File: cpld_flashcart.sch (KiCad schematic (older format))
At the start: 12 parts, among them J1 Micro_SD_Card, J2 GG_FrontPins, J3 GG_BackPins, J4 Conn_01x10_Female, U1 TXB0104PW, U2 AP2112K-3.3, U3 ATmega4809-A, U4 SST39SF040, U5 ATF1502AS-xAx44

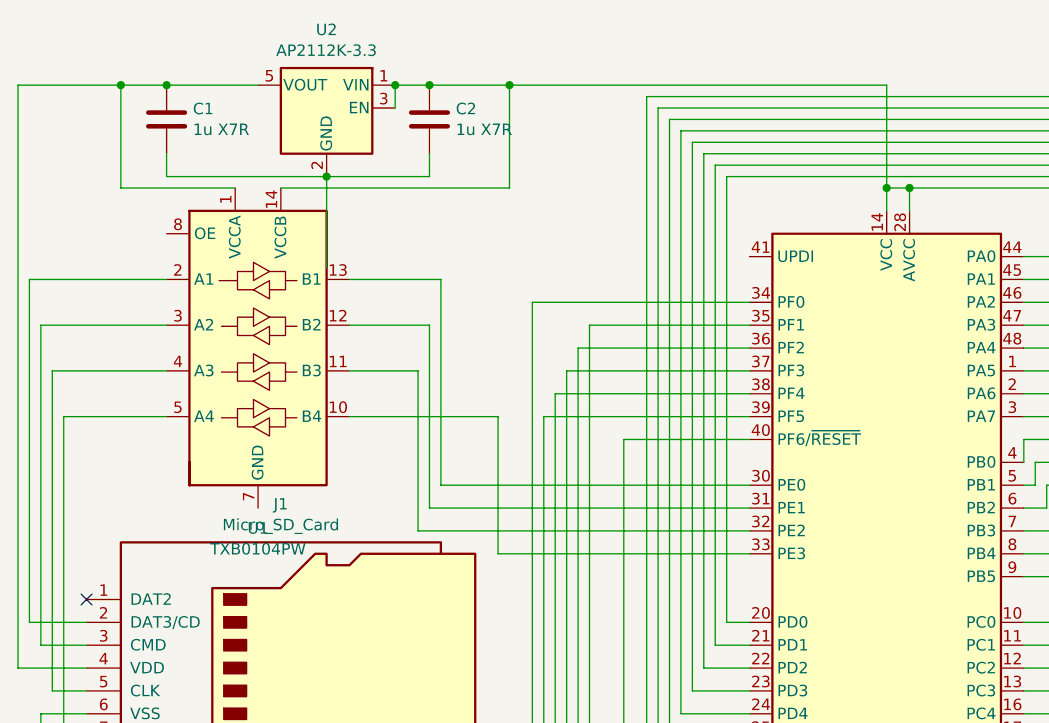
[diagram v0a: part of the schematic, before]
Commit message: Added CUPL code for mapper, and some changes to the schematic (which is definitely still incomplete).
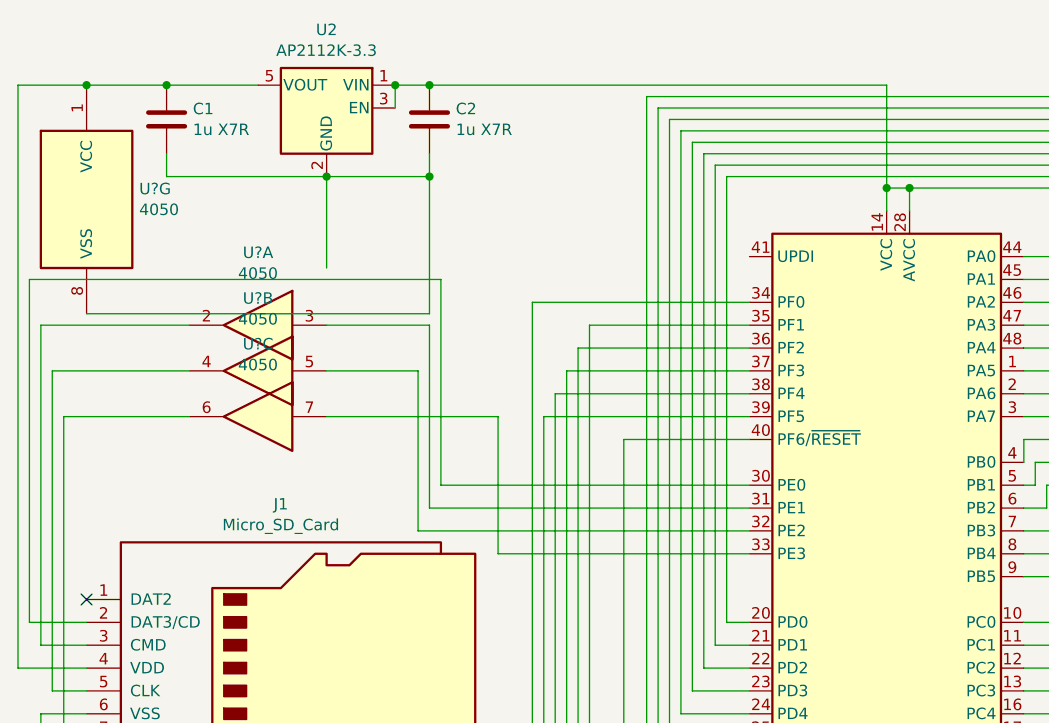
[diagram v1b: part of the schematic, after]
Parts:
- removed U1: TXB0104PW, Package_SO:TSSOP-14_4.4x5mm_P0.65mm, symbol Logic_LevelTranslator:TXB0104PW
- added U? (x4): 4050, symbol 4xxx:4050
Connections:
- net at U3.30 (PE0): now also J1.2 (DAT3/CD)
- net at U3.31 (PE1): now also U?.3
- net at U3.32 (PE2): now also U?.5
- net at U3.33 (PE3): now also U?.7
- net at C1.1, J1.4 (VDD), U2.5 (VOUT): now also U?.1 (VCC)
- net at J1.3 (CMD): now also U?.2
- net at J1.5 (CLK): now also U?.4
- net at J1.7 (DAT0): now also U?.6
- net at C1.2, C2.2, U2.2 (GND): now also U?.8 (VSS)
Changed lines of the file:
@@
 Connection ~ 1150 900
-Wire Wire Line
-	1150 900  950  900
 Wire Wire Line
 	1150 1300 1150 1200
@@
 Wire Wire Line
 	3450 3850 3700 3850
-$Comp
-L Logic_LevelTranslator:TXB0104PW U1
-U 1 1 60A4F48C
-P 1550 2050
-F 0 "U1" H 1550 1261 50  0000 C CNN
-F 1 "TXB0104PW" H 1550 1170 50  0000 C CNN
-F 2 "Package_SO:TSSOP-14_4.4x5mm_P0.65mm" H 1550 1300 50  0001 C CNN
-F 3 "http://www.ti.com/lit/ds/symlink/txb0104.pdf" H 1660 2145 50  0001 C CNN
-	1    1550 2050
+Wire Wire Line
+	800  3250 550  3250
+Wire Wire Line
+	550  3250 550  1750
+Wire Wire Line
+	600  1950 600  3350
+Wire Wire Line
+	600  3350 800  3350
+Wire Wire Line
+	800  3550 650  3550
+Wire Wire Line
+	650  3550 650  2150
+Wire Wire Line
+	700  2350 700  3750
+Wire Wire Line
+	700  3750 800  3750
+Wire Wire Line
+	3700 2650 2350 2650
+Wire Wire Line
+	2350 2650 2350 1750
+Wire Wire Line
+	3700 2750 2300 2750
+Wire Wire Line
+	2300 2750 2300 1950
+Wire Wire Line
+	2250 2150 2250 2850
+Wire Wire Line
+	2250 2850 3700 2850
+Wire Wire Line
+	3700 2950 2600 2950
+Wire Wire Line
+	2600 2950 2600 2350
+Wire Wire Line
+	550  1750 2350 1750
+$Comp
+L 4xxx:4050 U?
+U 1 1 60B9B079
+P 1550 1950
+F 0 "U?" H 1550 2267 50  0000 C CNN
+F 1 "4050" H 1550 2176 50  0000 C CNN
+F 2 "" H 1550 1950 50  0001 C CNN
+F 3 "http://www.intersil.com/content/dam/intersil/documents/cd40/cd4050bms.pdf" H 1550 1950 50  0001 C CNN
+	1    1550 1950
+	-1   0    0    -1
+$EndComp
+Wire Wire Line
+	1850 1950 2300 1950
+Wire Wire Line
+	600  1950 1250 1950
+$Comp
+L 4xxx:4050 U?
+U 2 1 60C12E35
+P 1550 2150
+F 0 "U?" H 1550 2467 50  0000 C CNN
+F 1 "4050" H 1550 2376 50  0000 C CNN
+F 2 "" H 1550 2150 50  0001 C CNN
+F 3 "http://www.intersil.com/content/dam/intersil/documents/cd40/cd4050bms.pdf" H 1550 2150 50  0001 C CNN
+	2    1550 2150
+	-1   0    0    -1
+$EndComp
+Wire Wire Line
+	1850 2150 2250 2150
+Wire Wire Line
+	650  2150 1250 2150
+$Comp
+L 4xxx:4050 U?
+U 3 1 60C8B5E7
+P 1550 2350
+F 0 "U?" H 1550 2667 50  0000 C CNN
+F 1 "4050" H 1550 2576 50  0000 C CNN
+F 2 "" H 1550 2350 50  0001 C CNN
+F 3 "http://www.intersil.com/content/dam/intersil/documents/cd40/cd4050bms.pdf" H 1550 2350 50  0001 C CNN
+	3    1550 2350
+	-1   0    0    -1
+$EndComp
+Wire Wire Line
+	1850 2350 2600 2350
+Wire Wire Line
+	700  2350 1250 2350
+Wire Wire Line
+	500  900  800  900
+Wire Wire Line
+	2300 900  4300 900
+$Comp
+L 4xxx:4050 U?
+U 7 1 60D09DAF
+P 800 1400
+F 0 "U?" H 1030 1446 50  0000 L CNN
+F 1 "4050" H 1030 1355 50  0000 L CNN
+F 2 "" H 800 1400 50  0001 C CNN
+F 3 "http://www.intersil.com/content/dam/intersil/documents/cd40/cd4050bms.pdf" H 800 1400 50  0001 C CNN
+	7    800  1400
 	1    0    0    -1
 $EndComp
-Wire Wire Line
-	800  3250 550  3250
-Wire Wire Line
-	550  3250 550  1750
-Wire Wire Line
-	550  1750 1150 1750
-Wire Wire Line
-	1150 1950 600  1950
-Wire Wire Line
-	600  1950 600  3350
-Wire Wire Line
-	600  3350 800  3350
-Wire Wire Line
-	800  3550 650  3550
-Wire Wire Line
-	650  3550 650  2150
-Wire Wire Line
-	650  2150 1150 2150
-Wire Wire Line
-	1150 2350 700  2350
-Wire Wire Line
-	700  2350 700  3750
-Wire Wire Line
-	700  3750 800  3750
-Wire Wire Line
-	3700 2650 2350 2650
-Wire Wire Line
-	2350 2650 2350 1750
-Wire Wire Line
-	2350 1750 1950 1750
-Wire Wire Line
-	3700 2750 2300 2750
-Wire Wire Line
-	2300 2750 2300 1950
-Wire Wire Line
-	2300 1950 1950 1950
-Wire Wire Line
-	1950 2150 2250 2150
-Wire Wire Line
-	2250 2150 2250 2850
-Wire Wire Line
-	2250 2850 3700 2850
-Wire Wire Line
-	3700 2950 2600 2950
-Wire Wire Line
-	2600 2950 2600 2350
-Wire Wire Line
-	2600 2350 1950 2350
-Wire Wire Line
-	1450 1350 950  1350
-Wire Wire Line
-	950  1350 950  900
-Connection ~ 950  900
-Wire Wire Line
-	950  900  500  900
-Wire Wire Line
-	2300 900  2650 900
-Wire Wire Line
-	1650 1350 2650 1350
-Wire Wire Line
-	2650 1350 2650 900
-Connection ~ 2650 900
-Wire Wire Line
-	2650 900  4300 900
+Connection ~ 800  900
+Wire Wire Line
+	800  900  1150 900
+Wire Wire Line
+	800  1900 2300 1900
+Wire Wire Line
+	2300 1900 2300 1300
+Connection ~ 2300 1300
 $EndSCHEMATC
